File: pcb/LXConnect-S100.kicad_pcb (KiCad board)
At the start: 2 copper layers, 32 x 82.5 mm, 16 parts, among them J1 LX, J11 CAN, J2 VP, J3 IN1, J4 IN2, J5 IN3, J6 IN4, J7 OAT, J8 SC, J9 PWR

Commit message: docu
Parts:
- added REF**: OSHW-Symbol_6.7x6mm_SilkScreen, Symbol:OSHW-Symbol_6.7x6mm_SilkScreen, B.Cu at (131.2, 86.4)
- added REF**: KiCad-Logo_5mm_SilkScreen, Symbol:KiCad-Logo_5mm_SilkScreen, B.Cu at (144.7, 86.4)
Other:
- board text added: "Keine Macht dem Kabelchaos!"
- board text added: "https://github.com/SoaringCircuits/LXConnect-S100"

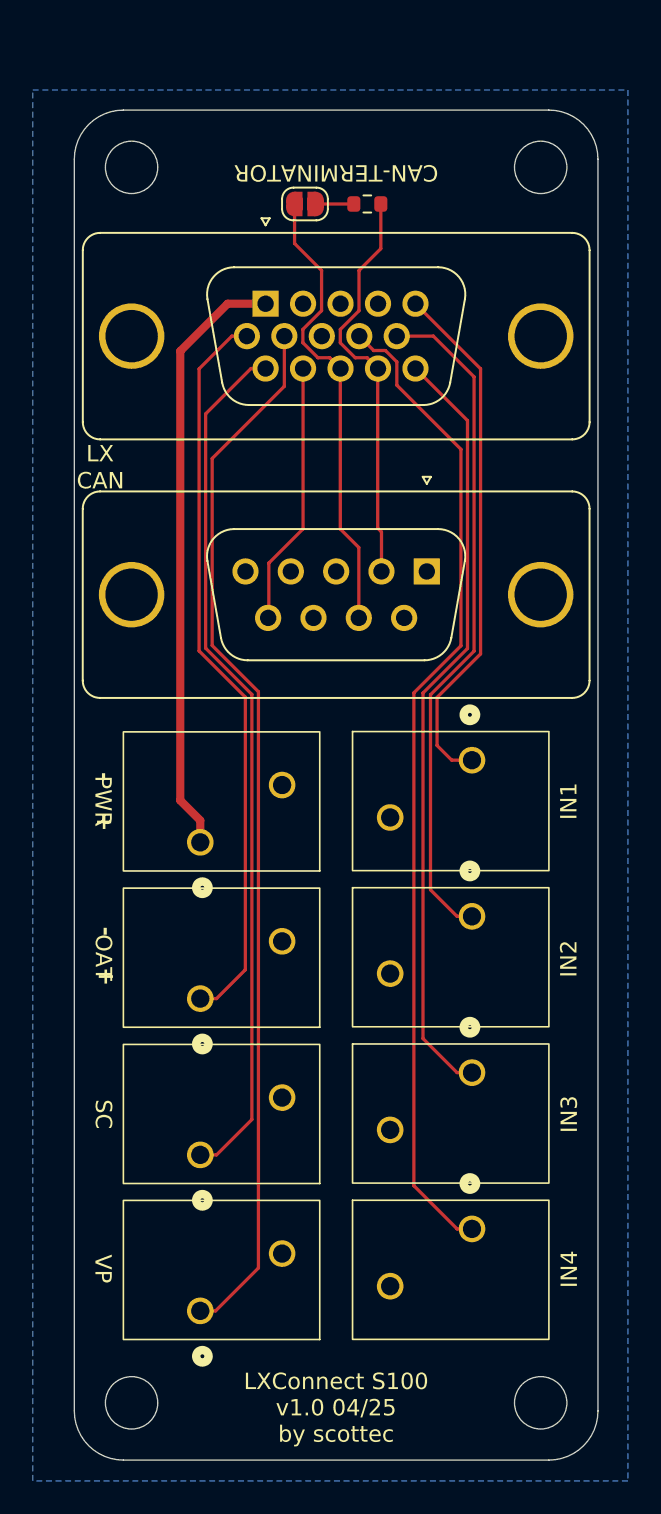
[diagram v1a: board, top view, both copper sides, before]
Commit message: pcb: docu on board
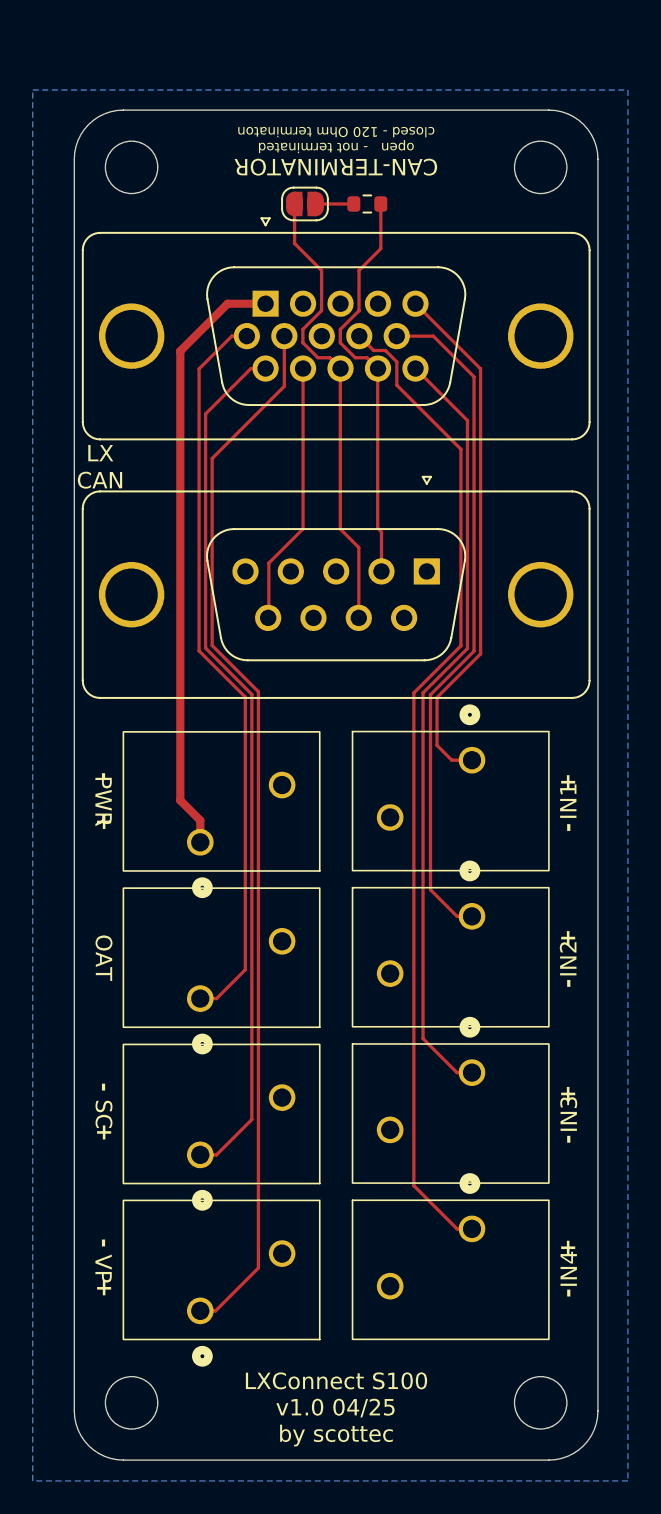
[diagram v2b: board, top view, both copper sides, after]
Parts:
- removed REF**: OSHW-Symbol_6.7x6mm_SilkScreen, Symbol:OSHW-Symbol_6.7x6mm_SilkScreen
- removed REF**: KiCad-Logo_5mm_SilkScreen, Symbol:KiCad-Logo_5mm_SilkScreen
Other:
- board text added: "open - not terminated closed - 120 Ohm terminaton"

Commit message: change connector to S100 to socket type to avoid shorts when not plugged
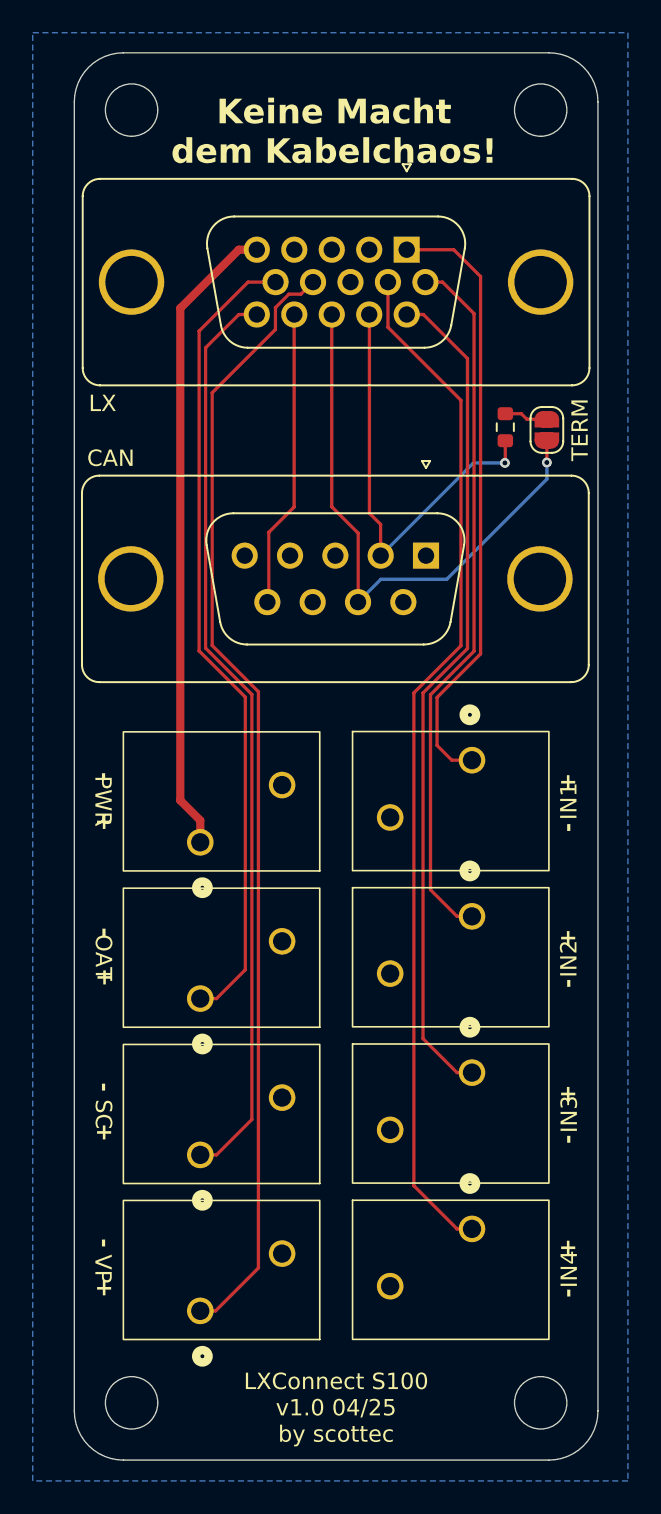
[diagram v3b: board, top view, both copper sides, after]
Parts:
- added REF**: KiCad-Logo2_5mm_SilkScreen, Symbol:KiCad-Logo2_5mm_SilkScreen, B.Cu at (139.7, 65.1)
- added REF**: OSHW-Logo_5.7x6mm_SilkScreen, Symbol:OSHW-Logo_5.7x6mm_SilkScreen, B.Cu at (139.6, 83.7)
- J1: footprint Connector_Dsub:DSUB-15-HD_Male_Vertical_P2.29x1.98mm_MountingHoles -> Connector_Dsub:DSUB-15-HD_Socket_Vertical_P2.29x1.98mm_MountingHoles
- J11: footprint Connector_Dsub:DSUB-9_Female_Vertical_P2.77x2.84mm_MountingHoles -> Connector_Dsub:DSUB-9_Socket_Vertical_P2.77x2.84mm_MountingHoles
- JP1: value CAN-TERMINATOR -> TERM
- moved JP1 20.2 mm to (152.6, 83.9), turned to -90 degrees
- moved R1 16.0 mm to (150.0, 83.7), turned to -90 degrees
- moved J1 9.23 mm to (144.0, 72.9)
- moved H1 3.50 mm to (127.2, 64.4)
- moved H2 3.50 mm to (152.2, 64.4)
- moved J11 0.97 mm to (145.2, 91.6)
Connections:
- J1 pad 0: (no net) -> GND
- J1 pad 1: /12V-IN -> /IN1
- J1 pad 10: /IN2 -> /OAT
- J1 pad 11: /SC -> /IN3
- J1 pad 12: /12V-OUT -> /CANL
- J1 pad 14: /CANL -> /12V-OUT
- J1 pad 15: /IN3 -> /SC
- J1 pad 4: GND -> unconnected-(J1-Pad4)
- J1 pad 5: /IN1 -> /12V-IN
- J1 pad 6: /OAT -> /IN2
- J1 pad 7: /VP -> /IN4
- J1 pad 9: /IN4 -> /VP
- J11 pad 0: (no net) -> GND
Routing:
- net /CANH: track 28.3 -> 35.3 mm, vias 0 -> 1
- net /IN1: track 32.3 -> 37.5 mm
- net /OAT: track 45.1 -> 49.6 mm
- net /VP: track 64.6 -> 69.0 mm
- net /IN3: track 47.2 -> 51.4 mm
- net /SC: track 53.2 -> 56.3 mm
- net /12V-IN: track 36.9 -> 39.3 mm
- net /IN4: track 60.8 -> 62.9 mm
- net /12V-OUT: track 16.1 -> 18.2 mm
- net /IN2: track 41.4 -> 43.3 mm
- net /CANL: track 25.0 -> 26.3 mm, vias 0 -> 1
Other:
- board size 32 x 82.5 mm -> 32 x 86 mm
- board text removed: "open - not terminated closed - 120 Ohm terminaton"
